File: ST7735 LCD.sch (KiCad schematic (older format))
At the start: 1 part, among them J36 LCD

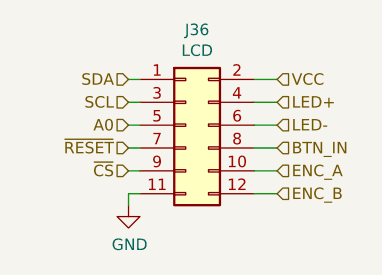
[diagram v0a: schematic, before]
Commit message: Added MISO signal to LCD connector. Improved LCD connector labels. Generated fabrication files.
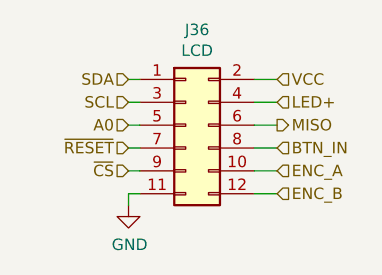
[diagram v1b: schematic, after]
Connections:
- net LED- renamed MISO
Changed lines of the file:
@@
 EESchema Schematic File Version 5
 LIBS:PrntrBoardV1-cache
-EELAYER 29 0
+EELAYER 30 0
 EELAYER END
 $Descr A4 11693 8268
@@
 Text HLabel 4100 1950 2    50   Input ~ 0
 LED+
-Text HLabel 4100 2050 2    50   Input ~ 0
-LED-
+Text HLabel 4100 2050 2    50   Output ~ 0
+MISO
 $Comp
 L power:GND #PWR086
